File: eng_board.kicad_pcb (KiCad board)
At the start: 6 copper layers, 20.2 x 31.4 mm, 54 parts, among them J1 Conn_01x12, J2 Conn_01x12, U1 LT3420, U12 TLV74318, U19 XS-LCC-01, U2 ADS7047, U5 ADS7047, U6 ADS7047, U7 TLV74325

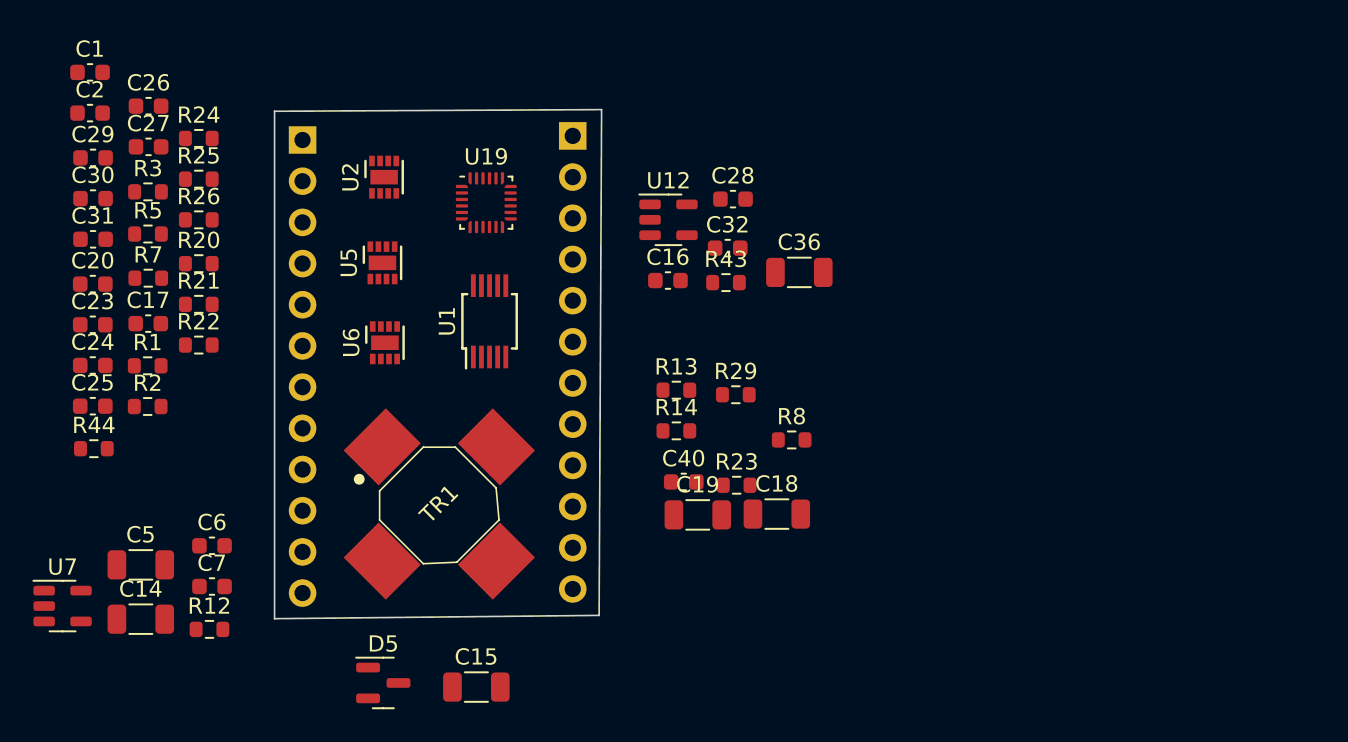
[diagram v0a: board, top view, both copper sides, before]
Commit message: change back to dual ADCs (with internal refs) for now. Leave the low cost ADCs to the future
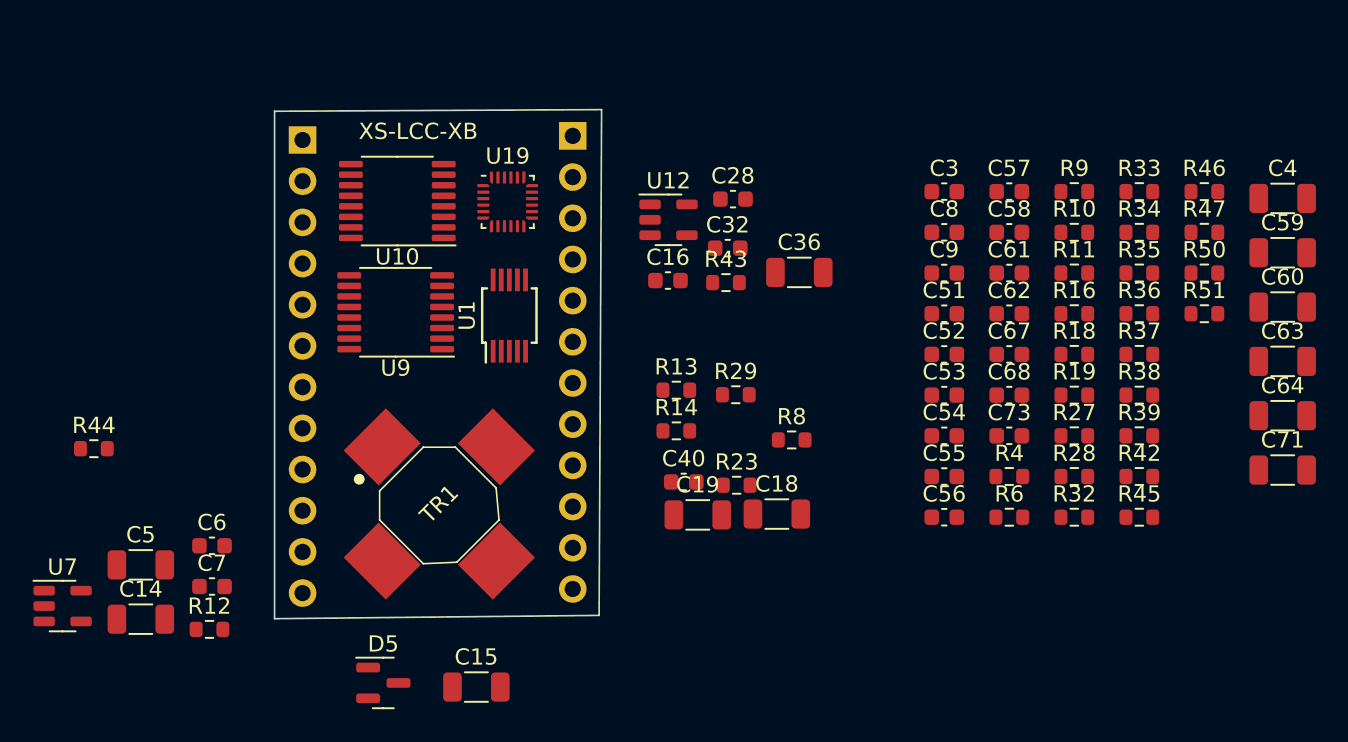
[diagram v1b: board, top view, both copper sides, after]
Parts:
- removed C1, C2, C23, C24, C27, C29: 2.2n, Capacitor_SMD:C_0603_1608Metric
- removed C17, C20, C25, C26, C30, C31: 0.1u, Capacitor_SMD:C_0603_1608Metric
- removed R1, R2, R20, R21, R25, R26: 51R, Resistor_SMD:R_0603_1608Metric
- removed R22, R24, R3, R5, R7: 22R, Resistor_SMD:R_0603_1608Metric
- removed U2, U5, U6: ADS7047, Package_DFN_QFN:VDFN-8-1EP_2x2mm_P0.5mm_EP0.9x1.7mm
- added C3: 0.01u, Capacitor_SMD:C_0603_1608Metric, F.Cu at (201.5, 92.1)
- added C4: 10u, Capacitor_SMD:C_1206_3216Metric, F.Cu at (222.3, 92.5)
- added C51: 2.2n, Capacitor_SMD:C_0603_1608Metric, F.Cu at (201.5, 99.7)
- added C52: 2.2n, Capacitor_SMD:C_0603_1608Metric, F.Cu at (201.5, 102.2)
- added C53: 2.2n, Capacitor_SMD:C_0603_1608Metric, F.Cu at (201.5, 104.7)
- added C54: 2.2n, Capacitor_SMD:C_0603_1608Metric, F.Cu at (201.5, 107.2)
- added C55: 2.2n, Capacitor_SMD:C_0603_1608Metric, F.Cu at (201.5, 109.7)
- added C56: 2.2n, Capacitor_SMD:C_0603_1608Metric, F.Cu at (201.5, 112.2)
- added C57: 2.2n, Capacitor_SMD:C_0603_1608Metric, F.Cu at (205.5, 92.1)
- added C58: 2.2n, Capacitor_SMD:C_0603_1608Metric, F.Cu at (205.5, 94.6)
- added C59: 10u, Capacitor_SMD:C_1206_3216Metric, F.Cu at (222.3, 95.9)
- added C60: 10u, Capacitor_SMD:C_1206_3216Metric, F.Cu at (222.3, 99.2)
- added C61: 0.1u, Capacitor_SMD:C_0603_1608Metric, F.Cu at (205.5, 97.1)
- added C62: 0.1u, Capacitor_SMD:C_0603_1608Metric, F.Cu at (205.5, 99.7)
- added C63: 10u, Capacitor_SMD:C_1206_3216Metric, F.Cu at (222.3, 102.6)
- added C64: 10u, Capacitor_SMD:C_1206_3216Metric, F.Cu at (222.3, 105.9)
- added C67: 0.1u, Capacitor_SMD:C_0603_1608Metric, F.Cu at (205.5, 102.2)
- added C68: 0.1u, Capacitor_SMD:C_0603_1608Metric, F.Cu at (205.5, 104.7)
- added C71: 10u, Capacitor_SMD:C_1206_3216Metric, F.Cu at (222.3, 109.3)
- added C73: 0.1u, Capacitor_SMD:C_0603_1608Metric, F.Cu at (205.5, 107.2)
- added C8: 0.1u, Capacitor_SMD:C_0603_1608Metric, F.Cu at (201.5, 94.6)
- added C9: 0.01u, Capacitor_SMD:C_0603_1608Metric, F.Cu at (201.5, 97.1)
- added R10: 0R, Resistor_SMD:R_0603_1608Metric, F.Cu at (209.5, 94.6)
- added R11: 0R, Resistor_SMD:R_0603_1608Metric, F.Cu at (209.5, 97.1)
- added R16: 0R, Resistor_SMD:R_0603_1608Metric, F.Cu at (209.5, 99.7)
- added R18: 0R, Resistor_SMD:R_0603_1608Metric, F.Cu at (209.5, 102.2)
- added R19: 0R, Resistor_SMD:R_0603_1608Metric, F.Cu at (209.5, 104.7)
- added R27: 1.99M, Resistor_SMD:R_0603_1608Metric, F.Cu at (209.5, 107.2)
- added R28: 10.01K, Resistor_SMD:R_0603_1608Metric, F.Cu at (209.5, 109.7)
- added R32: 51R, Resistor_SMD:R_0603_1608Metric, F.Cu at (209.5, 112.2)
- added R33: 51R, Resistor_SMD:R_0603_1608Metric, F.Cu at (213.5, 92.1)
- added R34: 51R, Resistor_SMD:R_0603_1608Metric, F.Cu at (213.5, 94.6)
- added R35: 51R, Resistor_SMD:R_0603_1608Metric, F.Cu at (213.5, 97.1)
- added R36: 51R, Resistor_SMD:R_0603_1608Metric, F.Cu at (213.5, 99.7)
- added R37: 51R, Resistor_SMD:R_0603_1608Metric, F.Cu at (213.5, 102.2)
- added R38: 51R, Resistor_SMD:R_0603_1608Metric, F.Cu at (213.5, 104.7)
- added R39: 51R, Resistor_SMD:R_0603_1608Metric, F.Cu at (213.5, 107.2)
- added R4: 10.01K, Resistor_SMD:R_0603_1608Metric, F.Cu at (205.5, 109.7)
- added R42: 22R, Resistor_SMD:R_0603_1608Metric, F.Cu at (213.5, 109.7)
- added R45: 22R, Resistor_SMD:R_0603_1608Metric, F.Cu at (213.5, 112.2)
- added R46: 22R, Resistor_SMD:R_0603_1608Metric, F.Cu at (217.5, 92.1)
- added R47: 22R, Resistor_SMD:R_0603_1608Metric, F.Cu at (217.5, 94.6)
- added R50: 22R, Resistor_SMD:R_0603_1608Metric, F.Cu at (217.5, 97.1)
- added R51: 22R, Resistor_SMD:R_0603_1608Metric, F.Cu at (217.5, 99.7)
- added R6: 0R, Resistor_SMD:R_0603_1608Metric, F.Cu at (205.5, 112.2)
- added R9: 1.001K, Resistor_SMD:R_0603_1608Metric, F.Cu at (209.5, 92.1)
- added U10: AD7352, Package_SO:TSSOP-16_4.4x5mm_P0.65mm, F.Cu at (167.7, 92.7)
- added U9: AD7352, Package_SO:TSSOP-16_4.4x5mm_P0.65mm, F.Cu at (167.6, 99.6)
- moved U19 1.32 mm to (174.5, 92.8)
- moved U1 1.27 mm to (174.7, 99.8)
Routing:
- removed copper zone on In3.Cu, net Net-(U2-AINM)
